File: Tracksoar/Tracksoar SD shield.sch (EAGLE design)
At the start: 8 parts, among them U1 HEX_CONVERTER

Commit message: removed old shields
removed square shields and added values to shield passives
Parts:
- C1: value (none) -> 10uf
- C2: value (none) -> .1uf
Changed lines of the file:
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@@
 <part name="U$2" library="SparkFun-PowerIC" deviceset="LM3480IM4" device=""/>
 <part name="U1" library="SparkFun-DigitalIC" deviceset="HEX_CONVERTER" device=""/>
-<part name="C1" library="SparkFun-Passives" deviceset="CAP" device="0805"/>
-<part name="C2" library="SparkFun-Passives" deviceset="CAP" device="0805"/>
+<part name="C1" library="SparkFun-Passives" deviceset="CAP" device="0805" value="10uf"/>
+<part name="C2" library="SparkFun-Passives" deviceset="CAP" device="0805" value=".1uf"/>
 </parts>
 <sheets>

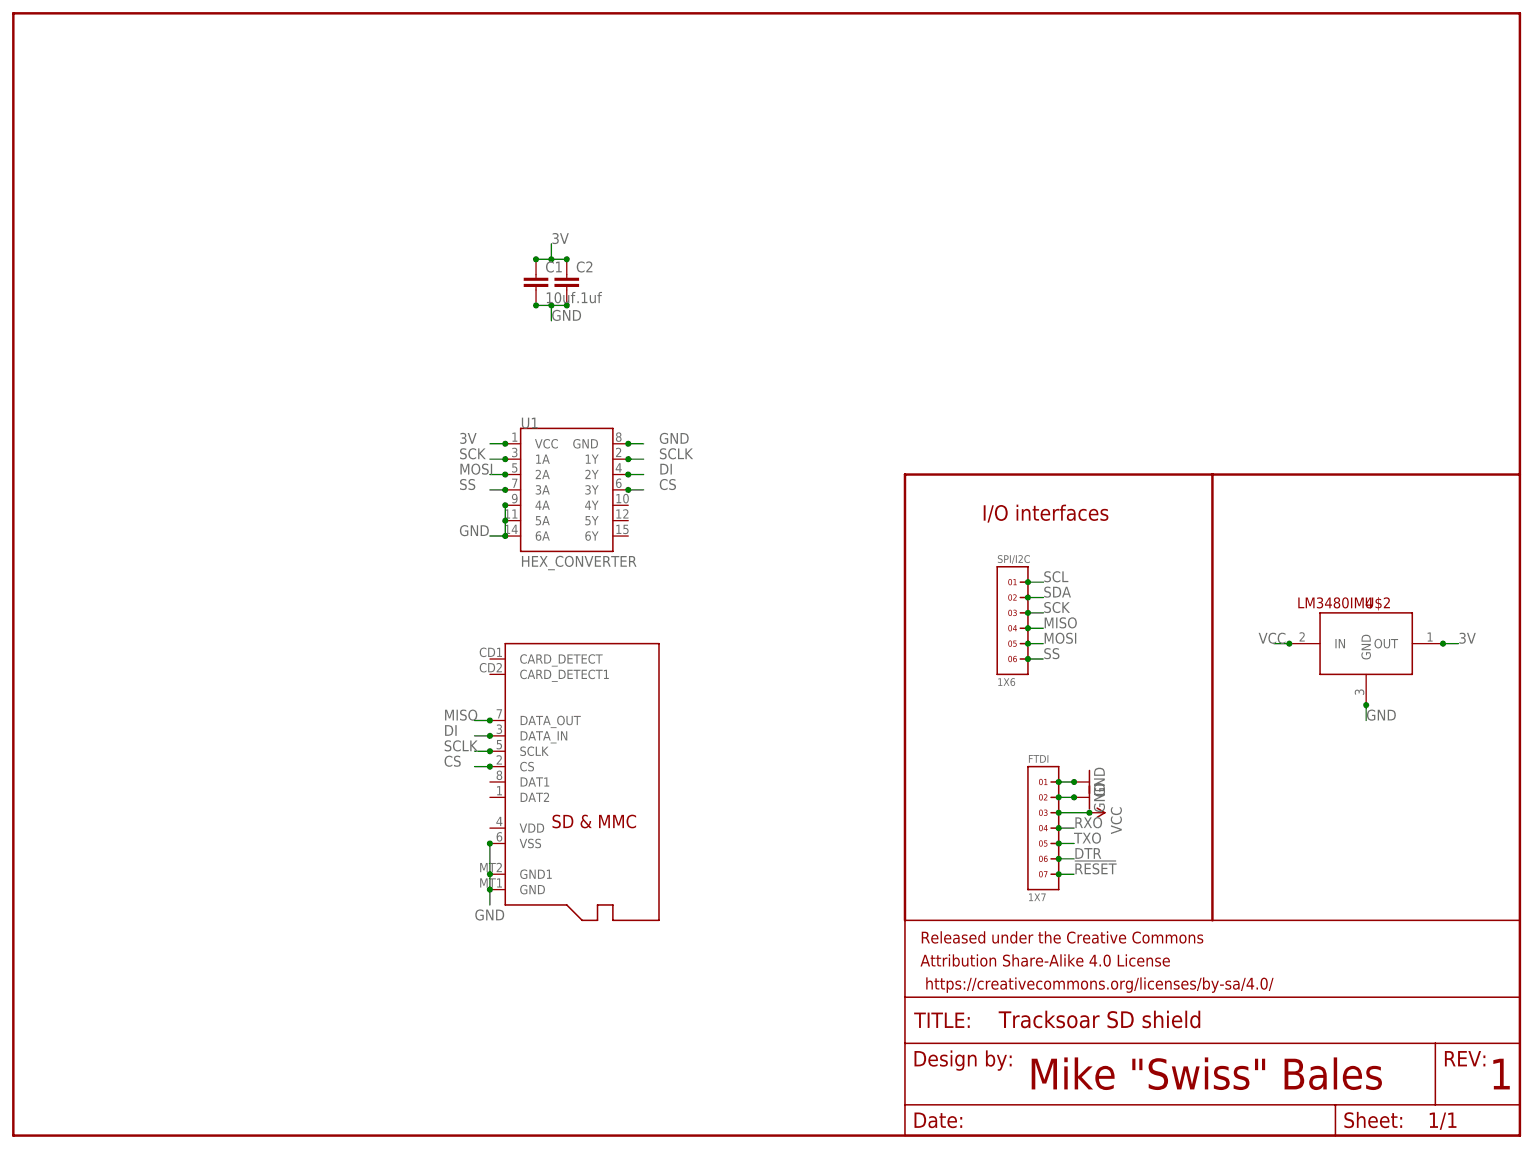
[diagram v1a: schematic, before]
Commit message: replaced sd with eeprom
the atmega328p does not have enough SRAM to handle the Trackuino duties
and SD read / write. It has been replace with an ST Micro M24M02 2Mb
eeprom. This will result in much less RAM usage, a smaller BOM, lower
cost, and lower power usage. However it also means we lose portability
of storage and easy computer interfacing. We’ll look at revising this
in future versions.
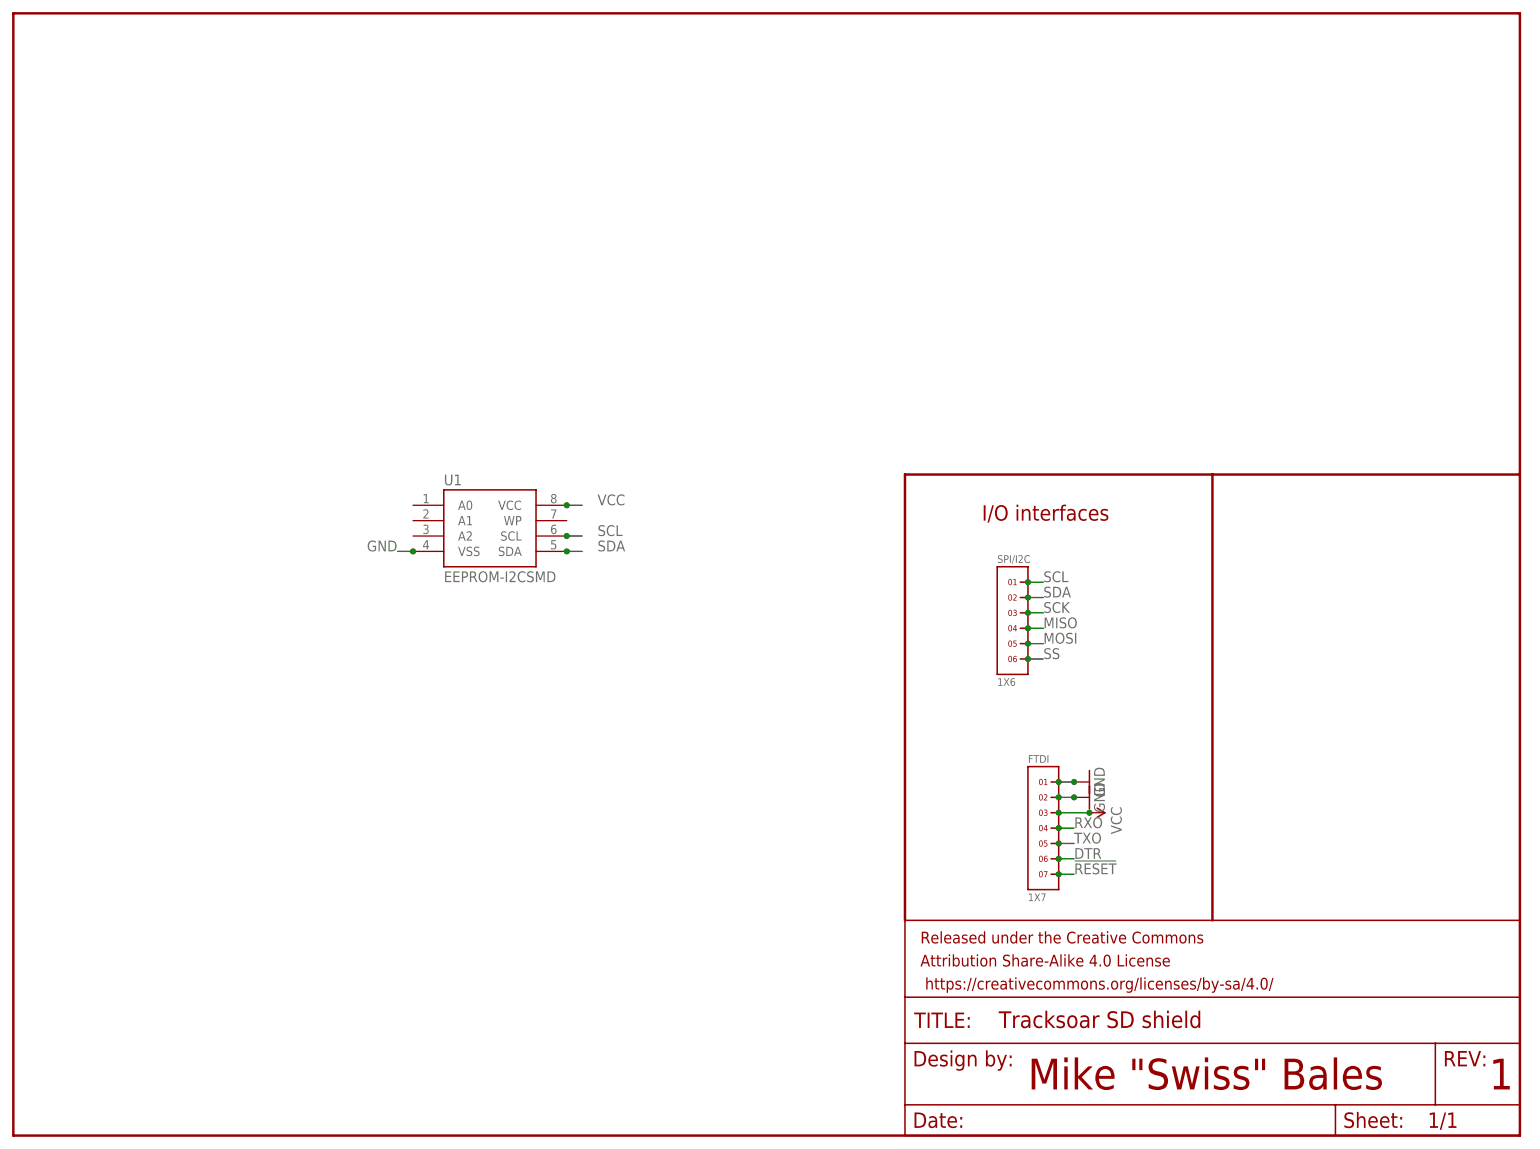
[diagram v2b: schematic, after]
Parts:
- removed C1: 10uf, SparkFun-Passives:CAP0805
- removed C2: .1uf, SparkFun-Passives:CAP0805
- removed U$1: MICROSD, adafruit:MICROSD
- removed U$2: LM3480IM4, SparkFun-PowerIC:LM3480IM4
- U1: value HEX_CONVERTER -> EEPROM-I2CSMD; device SparkFun-DigitalIC:HEX_CONVERTER -> SparkFun-DigitalIC:EEPROM-I2CSMD
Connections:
- removed net 3V: C1.1, C2.1, U$2.OUT, U1.VCC
- removed net CS: U$1.CS, U1.3Y
- removed net DI: U$1.DATA_IN, U1.2Y
- removed net SCLK: U$1.SCLK, U1.1Y
- net GND: now also U1.VSS; no longer C1.2, C2.2, U$1.GND, U$1.GND1, U$1.VSS, U$2.GND, U1.4A, U1.5A, U1.6A, U1.GND
- net MISO: no longer U$1.DATA_OUT
- net MOSI: no longer U1.2A
- net SCK: no longer U1.1A
- net SCL: now also U1.SCL
- net SDA: now also U1.SDA
- net SS: no longer U1.3A
- net VCC: now also U1.VCC; no longer U$2.IN
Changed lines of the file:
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@@
 <layers>
 <layer number="1" name="Top" color="4" fill="1" visible="no" active="no"/>
+<layer number="2" name="Route2" color="1" fill="3" visible="no" active="no"/>
+<layer number="3" name="Route3" color="4" fill="3" visible="no" active="no"/>
+<layer number="14" name="Route14" color="1" fill="6" visible="no" active="no"/>
+<layer number="15" name="Route15" color="4" fill="6" visible="no" active="no"/>
 <layer number="16" name="Bottom" color="1" fill="1" visible="no" active="no"/>
 <layer number="17" name="Pads" color="2" fill="1" visible="no" active="no"/>
@@
 <part name="FTDI" library="headers(2mm)" deviceset="1X7" device=""/>
 <part name="SPI/I2C" library="headers(2mm)" deviceset="1X6" device=""/>
-<part name="U$1" library="adafruit" deviceset="MICROSD" device=""/>
-<part name="U$2" library="SparkFun-PowerIC" deviceset="LM3480IM4" device=""/>
-<part name="U1" library="SparkFun-DigitalIC" deviceset="HEX_CONVERTER" device=""/>
-<part name="C1" library="SparkFun-Passives" deviceset="CAP" device="0805" value="10uf"/>
-<part name="C2" library="SparkFun-Passives" deviceset="CAP" device="0805" value=".1uf"/>
+<part name="U1" library="SparkFun-DigitalIC" deviceset="EEPROM-I2C" device="SMD"/>
 </parts>
 <sheets>
@@
 <instance part="FTDI" gate="G$1" x="170.18" y="50.8"/>
 <instance part="SPI/I2C" gate="G$1" x="165.1" y="83.82"/>
-<instance part="U$1" gate="G$1" x="96.52" y="60.96"/>
-<instance part="U$2" gate="G$1" x="223.52" y="81.28"/>
-<instance part="U1" gate="G$1" x="91.44" y="106.68"/>
-<instance part="C1" gate="G$1" x="86.36" y="139.7"/>
-<instance part="C2" gate="G$1" x="91.44" y="139.7"/>
+<instance part="U1" gate="G$1" x="78.74" y="99.06"/>
 </instances>
 <busses>
@@
 </segment>
 <segment>
-<pinref part="U$1" gate="G$1" pin="VSS"/>
-<wire x1="78.74" y1="48.26" x2="78.74" y2="43.18" width="0.1524" layer="91"/>
-<junction x="78.74" y="48.26"/>
-<pinref part="U$1" gate="G$1" pin="GND1"/>
-<junction x="78.74" y="43.18"/>
-<wire x1="78.74" y1="43.18" x2="78.74" y2="40.64" width="0.1524" layer="91"/>
-<pinref part="U$1" gate="G$1" pin="GND"/>
-<junction x="78.74" y="40.64"/>
-<wire x1="78.74" y1="40.64" x2="78.74" y2="38.1" width="0.1524" layer="91"/>
-<label x="76.2" y="35.56" size="1.778" layer="95"/>
-</segment>
-<segment>
-<pinref part="C1" gate="G$1" pin="2"/>
-<pinref part="C2" gate="G$1" pin="2"/>
-<wire x1="86.36" y1="137.16" x2="88.9" y2="137.16" width="0.1524" layer="91"/>
-<wire x1="88.9" y1="137.16" x2="91.44" y2="137.16" width="0.1524" layer="91"/>
-<wire x1="88.9" y1="137.16" x2="88.9" y2="134.62" width="0.1524" layer="91"/>
-<junction x="86.36" y="137.16"/>
-<junction x="88.9" y="137.16"/>
-<junction x="91.44" y="137.16"/>
-<label x="88.9" y="134.62" size="1.778" layer="95"/>
-</segment>
-<segment>
-<pinref part="U1" gate="G$1" pin="4A"/>
-<pinref part="U1" gate="G$1" pin="6A"/>
-<wire x1="81.28" y1="104.14" x2="81.28" y2="101.6" width="0.1524" layer="91"/>
-<wire x1="81.28" y1="101.6" x2="81.28" y2="99.06" width="0.1524" layer="91"/>
-<wire x1="81.28" y1="99.06" x2="78.74" y2="99.06" width="0.1524" layer="91"/>
-<junction x="81.28" y="104.14"/>
-<pinref part="U1" gate="G$1" pin="5A"/>
-<junction x="81.28" y="101.6"/>
-<junction x="81.28" y="99.06"/>
-<label x="73.66" y="99.06" size="1.778" layer="95"/>
-</segment>
-<segment>
-<pinref part="U1" gate="G$1" pin="GND"/>
-<wire x1="101.6" y1="114.3" x2="104.14" y2="114.3" width="0.1524" layer="91"/>
-<junction x="101.6" y="114.3"/>
-<label x="106.68" y="114.3" size="1.778" layer="95"/>
-</segment>
-<segment>
-<pinref part="U$2" gate="G$1" pin="GND"/>
-<wire x1="223.52" y1="71.12" x2="223.52" y2="68.58" width="0.1524" layer="91"/>
-<junction x="223.52" y="71.12"/>
-<label x="223.52" y="68.58" size="1.778" layer="95"/>
+<pinref part="U1" gate="G$1" pin="VSS"/>
+<wire x1="66.04" y1="96.52" x2="63.5" y2="96.52" width="0.1524" layer="91"/>
+<label x="58.42" y="96.52" size="1.778" layer="95"/>
+<junction x="66.04" y="96.52"/>
 </segment>
 </net>
@@
 </segment>
 <segment>
-<pinref part="U$2" gate="G$1" pin="IN"/>
-<wire x1="210.82" y1="81.28" x2="208.28" y2="81.28" width="0.1524" layer="91"/>
-<junction x="210.82" y="81.28"/>
-<label x="205.74" y="81.28" size="1.778" layer="95"/>
+<pinref part="U1" gate="G$1" pin="VCC"/>
+<wire x1="91.44" y1="104.14" x2="93.98" y2="104.14" width="0.1524" layer="91"/>
+<label x="96.52" y="104.14" size="1.778" layer="95"/>
+<junction x="91.44" y="104.14"/>
 </segment>
 </net>
@@
 <junction x="167.64" y="83.82"/>
 </segment>
-<segment>
-<pinref part="U$1" gate="G$1" pin="DATA_OUT"/>
-<wire x1="78.74" y1="68.58" x2="76.2" y2="68.58" width="0.1524" layer="91"/>
-<junction x="78.74" y="68.58"/>
-<label x="71.12" y="68.58" size="1.778" layer="95"/>
-</segment>
 </net>
 <net name="MOSI" class="0">
@@
 <junction x="167.64" y="81.28"/>
 </segment>
-<segment>
-<pinref part="U1" gate="G$1" pin="2A"/>
-<wire x1="81.28" y1="109.22" x2="78.74" y2="109.22" width="0.1524" layer="91"/>
-<junction x="81.28" y="109.22"/>
-<label x="73.66" y="109.22" size="1.778" layer="95"/>
-</segment>
 </net>
 <net name="SCK" class="0">
@@
 <junction x="167.64" y="86.36"/>
 </segment>
-<segment>
-<pinref part="U1" gate="G$1" pin="1A"/>
-<wire x1="81.28" y1="111.76" x2="78.74" y2="111.76" width="0.1524" layer="91"/>
-<junction x="81.28" y="111.76"/>
-<label x="73.66" y="111.76" size="1.778" layer="95"/>
-</segment>
 </net>
 <net name="SS" class="0">
@@
 <junction x="167.64" y="78.74"/>
 </segment>
-<segment>
-<pinref part="U1" gate="G$1" pin="3A"/>
-<wire x1="81.28" y1="106.68" x2="78.74" y2="106.68" width="0.1524" layer="91"/>
-<junction x="81.28" y="106.68"/>
-<label x="73.66" y="106.68" size="1.778" layer="95"/>
-</segment>
 </net>
 <net name="SDA" class="0">
@@
 <junction x="167.64" y="88.9"/>
 </segment>
+<segment>
+<pinref part="U1" gate="G$1" pin="SDA"/>
+<wire x1="91.44" y1="96.52" x2="93.98" y2="96.52" width="0.1524" layer="91"/>
+<label x="96.52" y="96.52" size="1.778" layer="95"/>
+<junction x="91.44" y="96.52"/>
+</segment>
 </net>
 <net name="SCL" class="0">
@@
 <junction x="167.64" y="91.44"/>
 </segment>
+<segment>
+<pinref part="U1" gate="G$1" pin="SCL"/>
+<wire x1="91.44" y1="99.06" x2="93.98" y2="99.06" width="0.1524" layer="91"/>
+<label x="96.52" y="99.06" size="1.778" layer="95"/>
+<junction x="91.44" y="99.06"/>
+</segment>
 </net>
 <net name="!RESET" class="0">
@@
 </segment>
 </net>
-<net name="3V" class="0">
-<segment>
-<pinref part="C1" gate="G$1" pin="1"/>
-<pinref part="C2" gate="G$1" pin="1"/>
-<wire x1="86.36" y1="144.78" x2="88.9" y2="144.78" width="0.1524" layer="91"/>
-<wire x1="88.9" y1="144.78" x2="91.44" y2="144.78" width="0.1524" layer="91"/>
-<wire x1="88.9" y1="144.78" x2="88.9" y2="147.32" width="0.1524" layer="91"/>
-<junction x="86.36" y="144.78"/>
-<junction x="91.44" y="144.78"/>
-<junction x="88.9" y="144.78"/>
-<label x="88.9" y="147.32" size="1.778" layer="95"/>
-</segment>
-<segment>
-<pinref part="U1" gate="G$1" pin="VCC"/>
-<wire x1="81.28" y1="114.3" x2="78.74" y2="114.3" width="0.1524" layer="91"/>
-<junction x="81.28" y="114.3"/>
-<label x="73.66" y="114.3" size="1.778" layer="95"/>
-</segment>
-<segment>
-<pinref part="U$2" gate="G$1" pin="OUT"/>
-<wire x1="236.22" y1="81.28" x2="238.76" y2="81.28" width="0.1524" layer="91"/>
-<junction x="236.22" y="81.28"/>
-<label x="238.76" y="81.28" size="1.778" layer="95"/>
-</segment>
-</net>
-<net name="SCLK" class="0">
-<segment>
-<pinref part="U1" gate="G$1" pin="1Y"/>
-<wire x1="101.6" y1="111.76" x2="104.14" y2="111.76" width="0.1524" layer="91"/>
-<junction x="101.6" y="111.76"/>
-<label x="106.68" y="111.76" size="1.778" layer="95"/>
-</segment>
-<segment>
-<pinref part="U$1" gate="G$1" pin="SCLK"/>
-<wire x1="78.74" y1="63.5" x2="76.2" y2="63.5" width="0.1524" layer="91"/>
-<junction x="78.74" y="63.5"/>
-<label x="71.12" y="63.5" size="1.778" layer="95"/>
-</segment>
-</net>
-<net name="DI" class="0">
-<segment>
-<pinref part="U1" gate="G$1" pin="2Y"/>
-<wire x1="101.6" y1="109.22" x2="104.14" y2="109.22" width="0.1524" layer="91"/>
-<junction x="101.6" y="109.22"/>
-<label x="106.68" y="109.22" size="1.778" layer="95"/>
-</segment>
-<segment>
-<pinref part="U$1" gate="G$1" pin="DATA_IN"/>
-<wire x1="78.74" y1="66.04" x2="76.2" y2="66.04" width="0.1524" layer="91"/>
-<junction x="78.74" y="66.04"/>
-<label x="71.12" y="66.04" size="1.778" layer="95"/>
-</segment>
-</net>
-<net name="CS" class="0">
-<segment>
-<pinref part="U1" gate="G$1" pin="3Y"/>
-<wire x1="101.6" y1="106.68" x2="104.14" y2="106.68" width="0.1524" layer="91"/>
-<junction x="101.6" y="106.68"/>
-<label x="106.68" y="106.68" size="1.778" layer="95"/>
-</segment>
-<segment>
-<pinref part="U$1" gate="G$1" pin="CS"/>
-<wire x1="78.74" y1="60.96" x2="76.2" y2="60.96" width="0.1524" layer="91"/>
-<junction x="78.74" y="60.96"/>
-<label x="71.12" y="60.96" size="1.778" layer="95"/>
-</segment>
-</net>
